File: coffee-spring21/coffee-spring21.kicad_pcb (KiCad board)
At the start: 4 copper layers, 57.5 x 68.7 mm, 55 parts, among them J1 AudioPlug3, SW1 SW_SPDT, U1 MAX2750AUA+, U11 SMA_PCB_Edge_Mount, U2 Opamp_Quad_Generic, U5 SMA_PCB_Edge_Mount, U6 SMA_PCB_Edge_Mount, U9 ADE-3G+

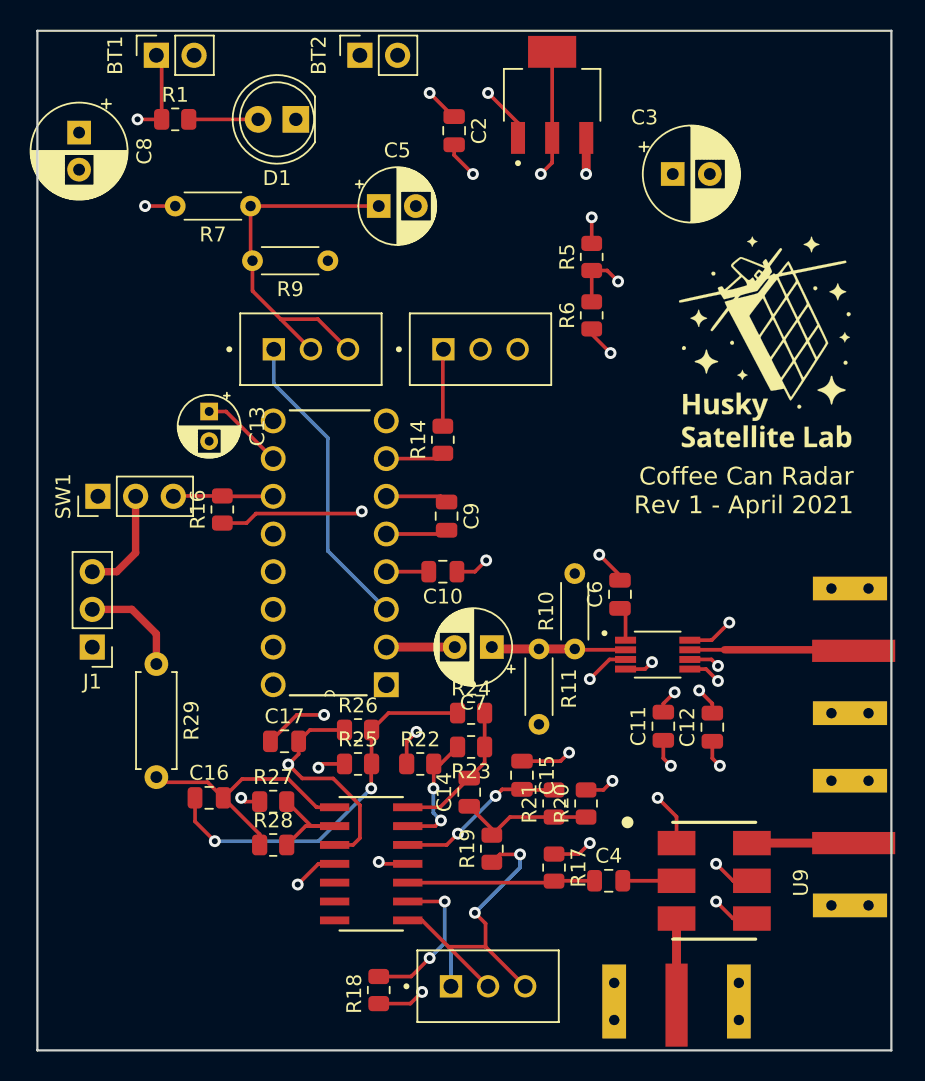
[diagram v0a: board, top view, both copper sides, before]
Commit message: Modified CCR layout
Added through hold resistors, power and ground terminals for SMA PA and LNA.
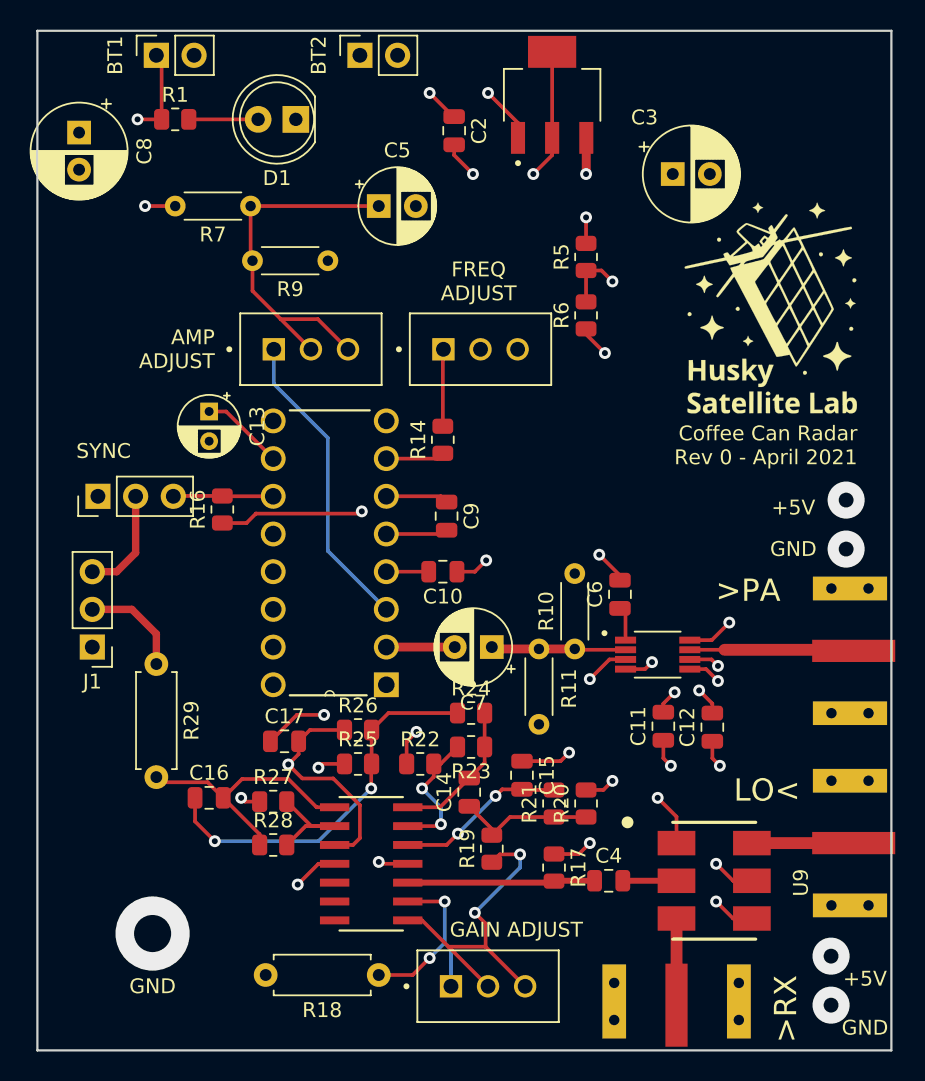
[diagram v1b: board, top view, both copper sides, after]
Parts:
- R16: value 100k -> 10k
- R18: footprint Resistor_SMD:R_0805_2012Metric -> Resistor_THT:R_Axial_DIN0207_L6.3mm_D2.5mm_P7.62mm_Horizontal
- moved G*** 2.32 mm to (169.4, 73.2)
- moved R18 1.02 mm to (143.0, 118.1), turned to 180 degrees
- moved R5 0.38 mm to (157.0, 69.7)
- moved R6 0.38 mm to (157.0, 73.7)
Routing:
- net 5V_OUT: track 214.5 -> 260.6 mm, vias 15 -> 16
- net Net-(R22-Pad2): track 8.50 -> 9.28 mm
- net 12V_OUT: track 100.8 -> 101.6 mm
- net GND: track 40.4 -> 40.6 mm, vias 13 -> 16
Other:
- board text added: "+5V"
- board text added: ">PA"
- board text added: ">RX"
- board text added: "AMP ADJUST"
- board text added: "Coffee Can Radar Rev 0 - April 2021"
- board text added: "FREQ ADJUST"
- board text added: "GAIN ADJUST"
- board text added: "GND"
- board text added: "LO<"
- board text added: "SYNC"
- board text removed: "Coffee Can Radar Rev 1 - April 2021"

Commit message: Board edits before fabricating
Via stitching, unused op-amp arrangement
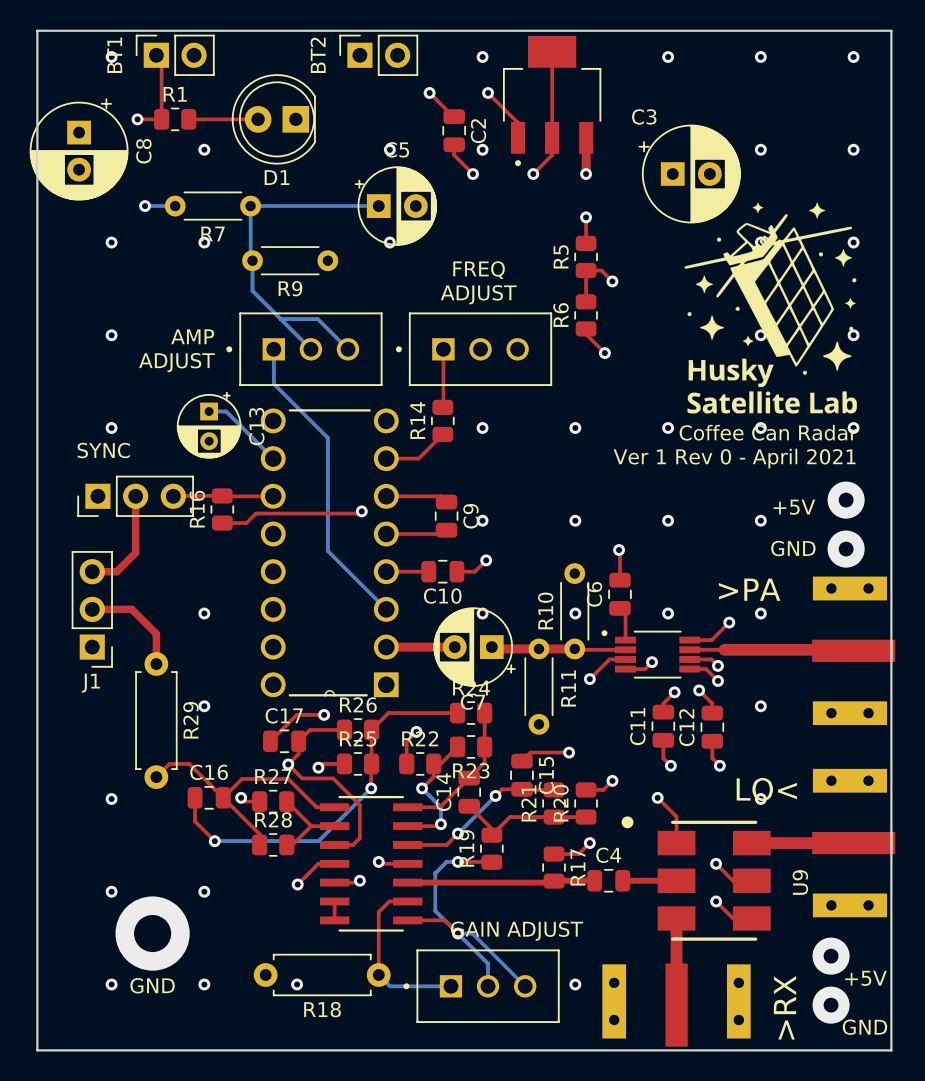
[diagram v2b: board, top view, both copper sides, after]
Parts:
- moved R14 1.27 mm to (147.3, 80.8)
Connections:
- U2 pad 12: (no net) -> 5V_OUT
- U2 pad 13: (no net) -> Net-(U2-Pad13)
- U2 pad 14: (no net) -> Net-(U2-Pad13)
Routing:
- net Net-(R18-Pad1): track 13.8 -> 11.7 mm, vias 2 -> 0
- net 5V_OUT: track 260.6 -> 262.4 mm, vias 16 -> 17
- net Net-(C16-Pad2): track 17.4 -> 19.0 mm
- net Net-(R27-Pad2): track 7.67 -> 6.09 mm
- net Net-(U2-Pad13): track 0.00 -> 1.27 mm
- net Net-(R14-Pad2): track 5.20 -> 3.99 mm
- net 12V_OUT: track 101.6 -> 100.6 mm
- net Net-(G1-Pad7): track 3.96 -> 4.48 mm
- net GND: track 40.6 -> 40.7 mm, vias 16 -> 59
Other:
- board text added: "Coffee Can Radar Ver 1 Rev 0 - April 2021"
- board text removed: "Coffee Can Radar Rev 0 - April 2021"
